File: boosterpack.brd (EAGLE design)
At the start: 76.5 x 55.9 mm, 38 parts, among them J1 POWERPOLE_DOUBLE, J2 PHOENIXSCREWTERMINAL_2, J3 PHOENIXSCREWTERMINAL_2

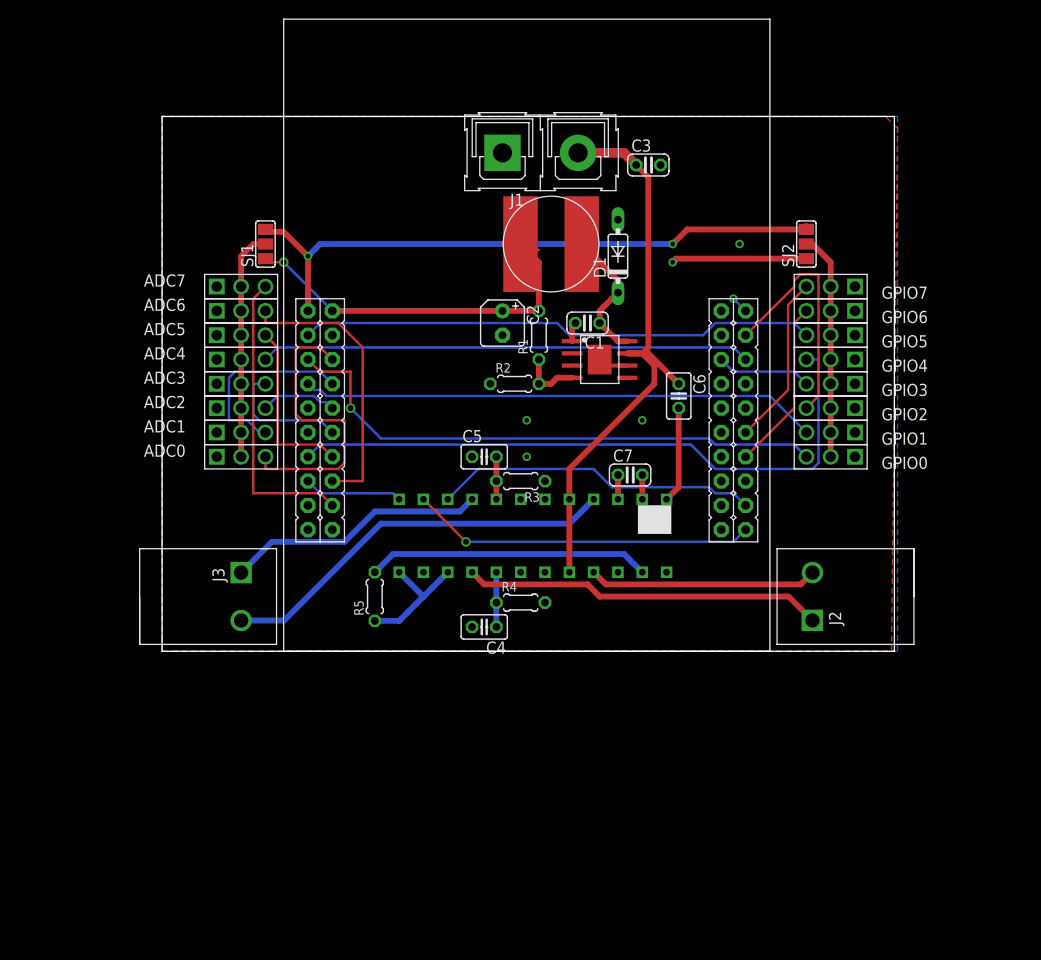
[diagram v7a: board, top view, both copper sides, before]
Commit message: fixed 3v3 not connecting to the motor drivers and rerouted some stuff
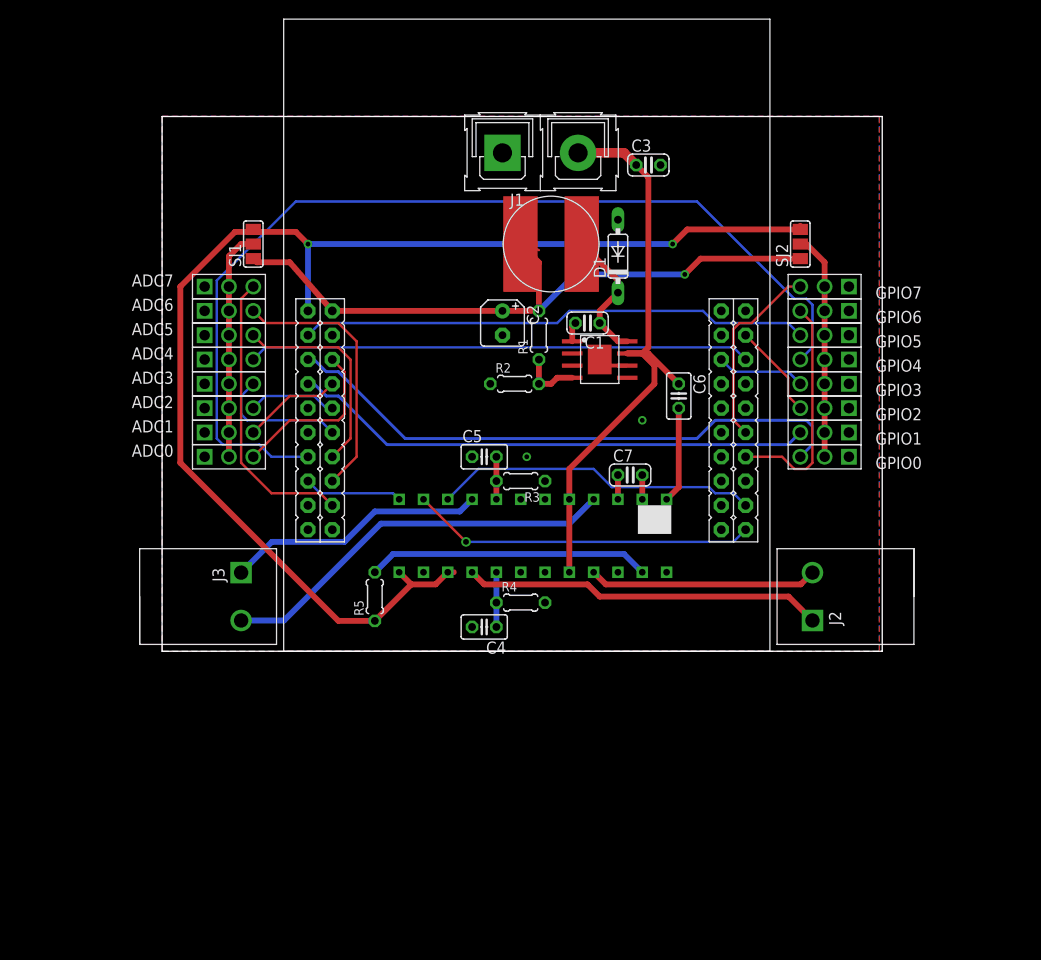
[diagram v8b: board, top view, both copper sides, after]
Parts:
- moved ADC0 1.27 mm to (14.6, 45.7)
- moved ADC1 1.27 mm to (14.6, 48.3)
- moved ADC2 1.27 mm to (14.6, 50.8)
- moved ADC3 1.27 mm to (14.6, 53.3)
- moved ADC4 1.27 mm to (14.6, 55.9)
- moved ADC5 1.27 mm to (14.6, 58.4)
- moved ADC6 1.27 mm to (14.6, 61.0)
- moved ADC7 1.27 mm to (14.6, 63.5)
- moved SJ1 1.27 mm to (19.7, 67.9)
- moved SJ2 0.64 mm to (76.8, 67.9)
- moved GPIO0 0.63 mm to (81.9, 45.7)
- moved GPIO1 0.63 mm to (81.9, 48.3)
- moved GPIO2 0.63 mm to (81.9, 50.8)
- moved GPIO3 0.63 mm to (81.9, 53.3)
- moved GPIO4 0.63 mm to (81.9, 55.9)
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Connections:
- removed net N$16: SJ1.3, SJ2.3, U$1.3.3V
- net +3V3: now also SJ1.3, SJ2.3, U$1.3.3V
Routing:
- net +3V3: track 13.3 -> 133.6 mm, vias 0 -> 2
- net N$16: track 64.9 -> 0.00 mm, vias 2 -> 0
- net N$2: track 67.2 -> 103.2 mm
- net +5V: track 55.6 -> 72.3 mm, vias 2 -> 1
- net GPIO2: track 25.1 -> 9.99 mm
- net N$1: track 30.9 -> 17.6 mm
- net ADC1: track 20.4 -> 10.4 mm
- net N$6: track 17.9 -> 24.2 mm
- net ADC5: track 18.2 -> 22.2 mm
- net GPIO0: track 58.5 -> 60.9 mm, vias 1 -> 0
- net N$8: track 17.9 -> 20.1 mm
- net N$4: track 29.6 -> 27.8 mm
- net GND: track 5.31 -> 3.51 mm, vias 5 -> 2
- net ADC2: track 8.04 -> 9.31 mm
- net N$13: track 51.2 -> 52.5 mm
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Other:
- board size 76.5 x 55.9 mm -> 75.2 x 55.9 mm
